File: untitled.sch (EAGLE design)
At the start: 25 parts

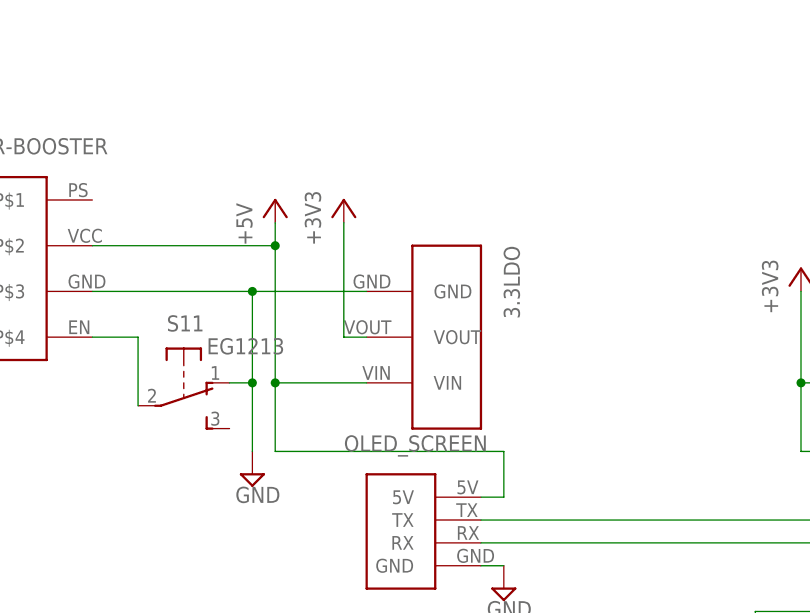
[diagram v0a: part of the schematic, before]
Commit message: Use regulator part from eagle library
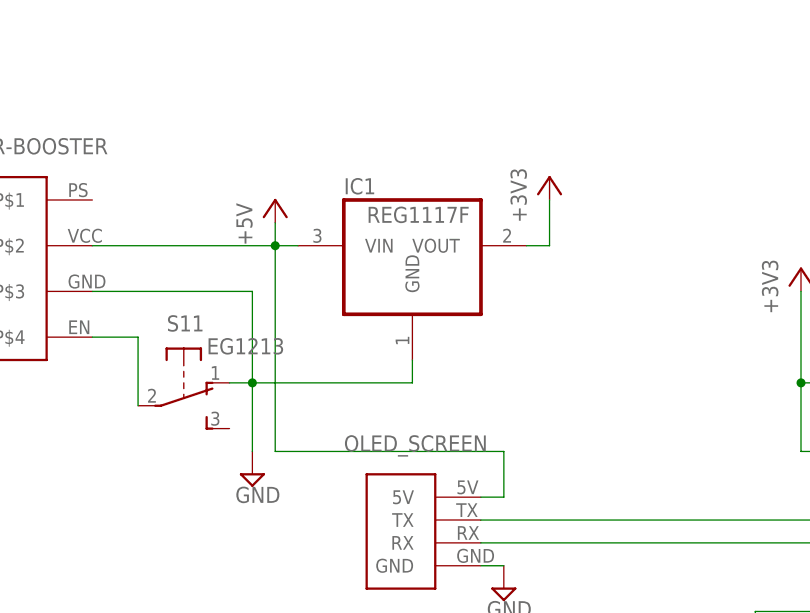
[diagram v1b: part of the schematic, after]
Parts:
- removed 3.3LDO: LDO1117-33, ldo1117-33:LDO1117-33
- added IC1: REG1117F, burr-brown:REG1117F
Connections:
- net +3V3: now also IC1.VOUT; no longer 3.3LDO.VOUT
- net +5V: now also IC1.VIN; no longer 3.3LDO.VIN
- net GND: now also IC1.GND; no longer 3.3LDO.GND
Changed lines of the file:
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@@
 <part name="OLED_SCREEN" library="4dScreen" deviceset="4DSCREEN" device=""/>
 <part name="LIPOCHARGER-BOOSTER" library="SFLipoPack" deviceset="SFLIPO" device=""/>
-<part name="3.3LDO" library="ldo1117-33" deviceset="LDO1117-33" device=""/>
 <part name="5WAYSWITCH" library="5-wayswitch" deviceset="5-WAYSWITCH" device=""/>
 <part name="EEPROM" library="adafruit" deviceset="DS1307" device=""/>
@@
 <part name="SUPPLY9" library="supply2" deviceset="GND" device=""/>
 <part name="+3V9" library="supply1" deviceset="+3V3" device=""/>
+<part name="IC1" library="burr-brown" deviceset="REG1117" device="F"/>
 </parts>
 <sheets>
@@
 <instance part="OLED_SCREEN" gate="G$1" x="-68.58" y="68.58"/>
 <instance part="LIPOCHARGER-BOOSTER" gate="G$1" x="-111.76" y="96.52"/>
-<instance part="3.3LDO" gate="G$1" x="-66.04" y="88.9" rot="R270"/>
 <instance part="5WAYSWITCH" gate="G$1" x="-71.12" y="0"/>
 <instance part="EEPROM" gate="G$1" x="165.1" y="27.94"/>
@@
 <instance part="SUPPLY6" gate="GND" x="165.1" y="10.16"/>
 <instance part="P+2" gate="1" x="-83.82" y="104.14"/>
-<instance part="+3V1" gate="G$1" x="-76.2" y="104.14"/>
+<instance part="+3V1" gate="G$1" x="-53.34" y="106.68"/>
 <instance part="+3V2" gate="G$1" x="-109.22" y="33.02"/>
 <instance part="+3V3" gate="G$1" x="-25.4" y="96.52"/>
@@
 <instance part="SUPPLY9" gate="GND" x="-7.62" y="7.62"/>
 <instance part="+3V9" gate="G$1" x="-7.62" y="25.4"/>
+<instance part="IC1" gate="G$1" x="-68.58" y="99.06"/>
 </instances>
 <busses>
@@
 <wire x1="-86.36" y1="76.2" x2="-86.36" y2="83.82" width="0.1524" layer="91"/>
 <junction x="-86.36" y="83.82"/>
-<pinref part="3.3LDO" gate="G$1" pin="GND"/>
-<wire x1="-86.36" y1="93.98" x2="-73.66" y2="93.98" width="0.1524" layer="91"/>
-<junction x="-86.36" y="93.98"/>
+<pinref part="IC1" gate="G$1" pin="GND"/>
+<wire x1="-68.58" y1="86.36" x2="-68.58" y2="83.82" width="0.1524" layer="91"/>
+<wire x1="-68.58" y1="83.82" x2="-86.36" y2="83.82" width="0.1524" layer="91"/>
 </segment>
 <segment>
@@
 <pinref part="LIPOCHARGER-BOOSTER" gate="G$1" pin="P$2"/>
 <wire x1="-104.14" y1="99.06" x2="-83.82" y2="99.06" width="0.1524" layer="91"/>
-<wire x1="-83.82" y1="99.06" x2="-83.82" y2="83.82" width="0.1524" layer="91"/>
-<wire x1="-83.82" y1="83.82" x2="-73.66" y2="83.82" width="0.1524" layer="91"/>
-<pinref part="3.3LDO" gate="G$1" pin="VIN"/>
+<wire x1="-83.82" y1="99.06" x2="-83.82" y2="76.2" width="0.1524" layer="91"/>
 <junction x="-83.82" y="99.06"/>
 <pinref part="P+2" gate="1" pin="+5V"/>
 <wire x1="-83.82" y1="101.6" x2="-83.82" y2="99.06" width="0.1524" layer="91"/>
-<wire x1="-83.82" y1="83.82" x2="-83.82" y2="76.2" width="0.1524" layer="91"/>
 <wire x1="-83.82" y1="76.2" x2="-58.42" y2="76.2" width="0.1524" layer="91"/>
-<junction x="-83.82" y="83.82"/>
 <pinref part="OLED_SCREEN" gate="G$1" pin="5V"/>
 <wire x1="-58.42" y1="76.2" x2="-58.42" y2="71.12" width="0.1524" layer="91"/>
 <wire x1="-58.42" y1="71.12" x2="-60.96" y2="71.12" width="0.1524" layer="91"/>
+<pinref part="IC1" gate="G$1" pin="VIN"/>
+<wire x1="-81.28" y1="99.06" x2="-83.82" y2="99.06" width="0.1524" layer="91"/>
 </segment>
 </net>
 <net name="+3V3" class="0">
-<segment>
-<pinref part="+3V1" gate="G$1" pin="+3V3"/>
-<pinref part="3.3LDO" gate="G$1" pin="VOUT"/>
-<wire x1="-76.2" y1="101.6" x2="-76.2" y2="88.9" width="0.1524" layer="91"/>
-<wire x1="-76.2" y1="88.9" x2="-73.66" y2="88.9" width="0.1524" layer="91"/>
-</segment>
 <segment>
 <pinref part="I2C5" gate="G$1" pin="1"/>
@@
 <wire x1="-7.62" y1="22.86" x2="-7.62" y2="20.32" width="0.1524" layer="91"/>
 </segment>
-</net>
+<segment>
+<pinref part="IC1" gate="G$1" pin="VOUT"/>
+<pinref part="+3V1" gate="G$1" pin="+3V3"/>
+<wire x1="-55.88" y1="99.06" x2="-53.34" y2="99.06" width="0.1524" layer="91"/>
+<wire x1="-53.34" y1="99.06" x2="-53.34" y2="104.14" width="0.1524" layer="91"/>
+</segment>
+</net>

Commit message: Lots of improvements
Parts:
- IC1: value REG1117F -> REG1117X; device burr-brown:REG1117F -> burr-brown:REG1117X
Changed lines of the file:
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@@
 <grid distance="0.1" unitdist="inch" unit="inch" style="lines" multiple="1" display="no" altdistance="0.01" altunitdist="inch" altunit="inch"/>
 <layers>
-<layer number="1" name="Top" color="4" fill="1" visible="no" active="no"/>
-<layer number="16" name="Bottom" color="1" fill="1" visible="no" active="no"/>
-<layer number="17" name="Pads" color="2" fill="1" visible="no" active="no"/>
-<layer number="18" name="Vias" color="2" fill="1" visible="no" active="no"/>
-<layer number="19" name="Unrouted" color="6" fill="1" visible="no" active="no"/>
-<layer number="20" name="Dimension" color="15" fill="1" visible="no" active="no"/>
-<layer number="21" name="tPlace" color="7" fill="1" visible="no" active="no"/>
-<layer number="22" name="bPlace" color="7" fill="1" visible="no" active="no"/>
-<layer number="23" name="tOrigins" color="15" fill="1" visible="no" active="no"/>
-<layer number="24" name="bOrigins" color="15" fill="1" visible="no" active="no"/>
-<layer number="25" name="tNames" color="7" fill="1" visible="no" active="no"/>
-<layer number="26" name="bNames" color="7" fill="1" visible="no" active="no"/>
-<layer number="27" name="tValues" color="7" fill="1" visible="no" active="no"/>
-<layer number="28" name="bValues" color="7" fill="1" visible="no" active="no"/>
+<layer number="1" name="Top" color="4" fill="1" visible="yes" active="no"/>
+<layer number="16" name="Bottom" color="1" fill="1" visible="yes" active="no"/>
+<layer number="17" name="Pads" color="2" fill="1" visible="yes" active="no"/>
+<layer number="18" name="Vias" color="2" fill="1" visible="yes" active="no"/>
+<layer number="19" name="Unrouted" color="6" fill="1" visible="yes" active="no"/>
+<layer number="20" name="Dimension" color="15" fill="1" visible="yes" active="no"/>
+<layer number="21" name="tPlace" color="7" fill="1" visible="yes" active="no"/>
+<layer number="22" name="bPlace" color="7" fill="1" visible="yes" active="no"/>
+<layer number="23" name="tOrigins" color="15" fill="1" visible="yes" active="no"/>
+<layer number="24" name="bOrigins" color="15" fill="1" visible="yes" active="no"/>
+<layer number="25" name="tNames" color="7" fill="1" visible="yes" active="no"/>
+<layer number="26" name="bNames" color="7" fill="1" visible="yes" active="no"/>
+<layer number="27" name="tValues" color="7" fill="1" visible="yes" active="no"/>
+<layer number="28" name="bValues" color="7" fill="1" visible="yes" active="no"/>
 <layer number="29" name="tStop" color="7" fill="3" visible="no" active="no"/>
 <layer number="30" name="bStop" color="7" fill="6" visible="no" active="no"/>
@@
 <layer number="35" name="tGlue" color="7" fill="4" visible="no" active="no"/>
 <layer number="36" name="bGlue" color="7" fill="5" visible="no" active="no"/>
-<layer number="37" name="tTest" color="7" fill="1" visible="no" active="no"/>
-<layer number="38" name="bTest" color="7" fill="1" visible="no" active="no"/>
+<layer number="37" name="tTest" color="7" fill="1" visible="yes" active="no"/>
+<layer number="38" name="bTest" color="7" fill="1" visible="yes" active="no"/>
 <layer number="39" name="tKeepout" color="4" fill="11" visible="no" active="no"/>
 <layer number="40" name="bKeepout" color="1" fill="11" visible="no" active="no"/>
@@
 <layer number="44" name="Drills" color="7" fill="1" visible="no" active="no"/>
 <layer number="45" name="Holes" color="7" fill="1" visible="no" active="no"/>
-<layer number="46" name="Milling" color="3" fill="1" visible="no" active="no"/>
-<layer number="47" name="Measures" color="7" fill="1" visible="no" active="no"/>
-<layer number="48" name="Document" color="7" fill="1" visible="no" active="no"/>
-<layer number="49" name="Reference" color="7" fill="1" visible="no" active="no"/>
-<layer number="50" name="dxf" color="7" fill="1" visible="no" active="no"/>
-<layer number="51" name="tDocu" color="7" fill="1" visible="no" active="no"/>
-<layer number="52" name="bDocu" color="7" fill="1" visible="no" active="no"/>
-<layer number="53" name="tGND_GNDA" color="7" fill="9" visible="no" active="no"/>
-<layer number="54" name="bGND_GNDA" color="1" fill="9" visible="no" active="no"/>
-<layer number="56" name="wert" color="7" fill="1" visible="no" active="no"/>
-<layer number="57" name="tCAD" color="7" fill="1" visible="no" active="no"/>
+<layer number="46" name="Milling" color="3" fill="1" visible="yes" active="no"/>
+<layer number="47" name="Measures" color="7" fill="1" visible="yes" active="no"/>
+<layer number="48" name="Document" color="7" fill="1" visible="yes" active="no"/>
+<layer number="49" name="Reference" color="7" fill="1" visible="yes" active="no"/>
+<layer number="50" name="dxf" color="7" fill="1" visible="yes" active="no"/>
+<layer number="51" name="tDocu" color="7" fill="1" visible="yes" active="no"/>
+<layer number="52" name="bDocu" color="7" fill="1" visible="yes" active="no"/>
+<layer number="53" name="tGND_GNDA" color="7" fill="9" visible="yes" active="no"/>
+<layer number="54" name="bGND_GNDA" color="1" fill="9" visible="yes" active="no"/>
+<layer number="56" name="wert" color="7" fill="1" visible="yes" active="no"/>
+<layer number="57" name="tCAD" color="7" fill="1" visible="yes" active="no"/>
 <layer number="90" name="Modules" color="5" fill="1" visible="yes" active="yes"/>
 <layer number="91" name="Nets" color="2" fill="1" visible="yes" active="yes"/>
@@
 <part name="SUPPLY9" library="supply2" deviceset="GND" device=""/>
 <part name="+3V9" library="supply1" deviceset="+3V3" device=""/>
-<part name="IC1" library="burr-brown" deviceset="REG1117" device="F"/>
+<part name="IC1" library="burr-brown" deviceset="REG1117" device="X" value="REG1117X"/>
 </parts>
 <sheets>
